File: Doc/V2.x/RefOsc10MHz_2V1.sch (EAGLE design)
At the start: 82 parts, among them CON1 TYCO-AMP_USBUSB-B_SMT, CON2 HEADER-2X5SMD, CON3 SD-73100-0105, CON4 AVR-ISP-6SMD, CON5 AVR-JTAG-10SMD, CON6 HEADER-2X3SMD, CON7 MCX-J-P-X-RA-SM1, IC1 ATmega328-P, IC2 LC4032V_XXT44, IC3 74HCT221D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

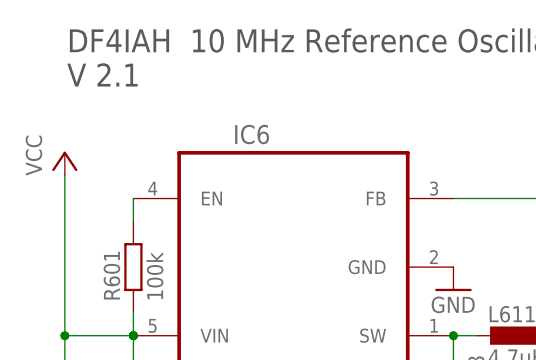
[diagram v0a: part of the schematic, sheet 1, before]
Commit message: avr_DF4IAH_Bootloader - Doc - Eagle: V2.1 - correction: CRS80 --> CRS08 (2)
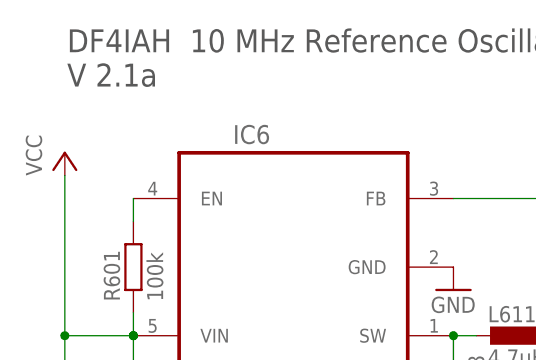
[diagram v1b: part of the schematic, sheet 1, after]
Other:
- note added: "DF4IAH 10 MHz Reference Oscillator V 2.1a"
- note removed: "DF4IAH 10 MHz Reference Oscillator V 2.1"
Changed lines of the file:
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@@
 <text x="198.12" y="145.034" size="1.016" layer="97">2.5 MHz out</text>
 <text x="5.334" y="291.846" size="2.54" layer="97">DF4IAH  10 MHz Reference Oscillator
-V 2.1</text>
+V 2.1a</text>
 <text x="59.436" y="144.018" size="1.778" layer="97">USB Disconnect</text>
 <text x="102.616" y="122.936" size="1.778" layer="97">USB D-</text>

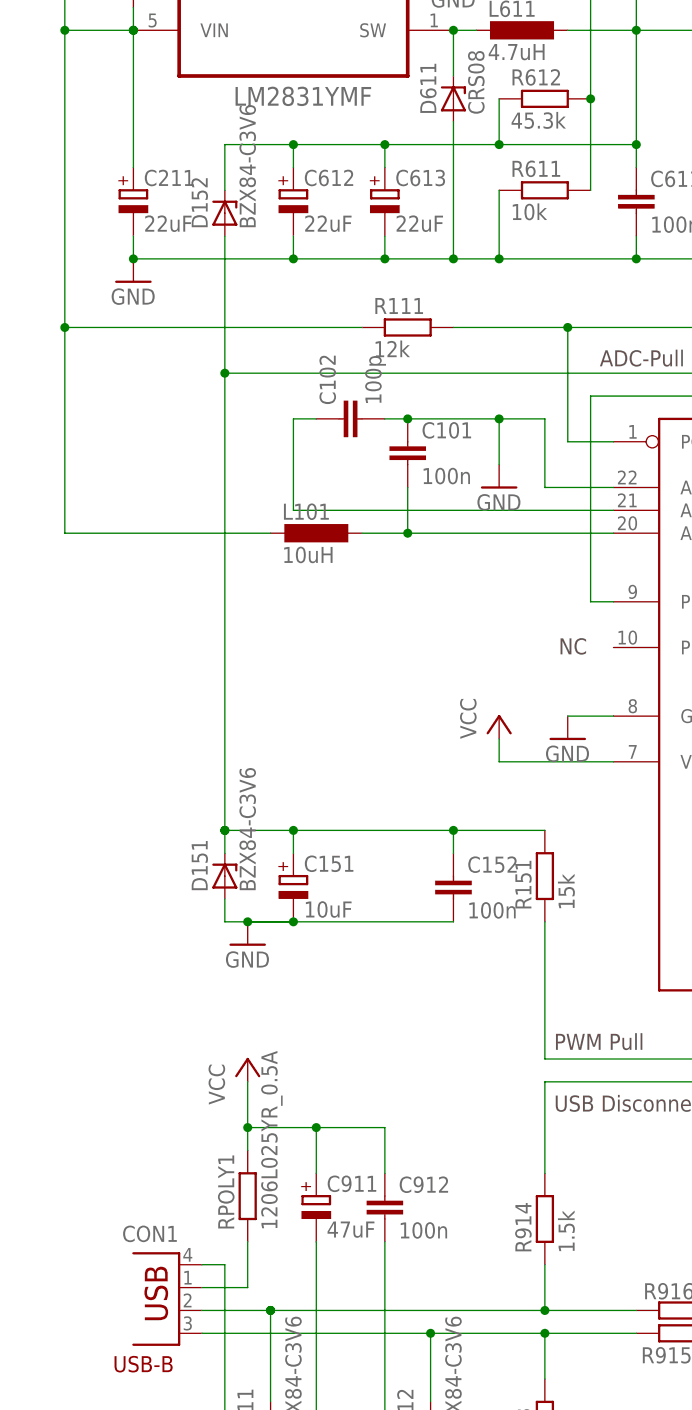
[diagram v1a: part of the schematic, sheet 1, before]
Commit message: avr_DF4IAH_Bootloader - Doc - Eagle: V2.1/V2.2 - removed elkos and replaced it by C0805 MLCCs
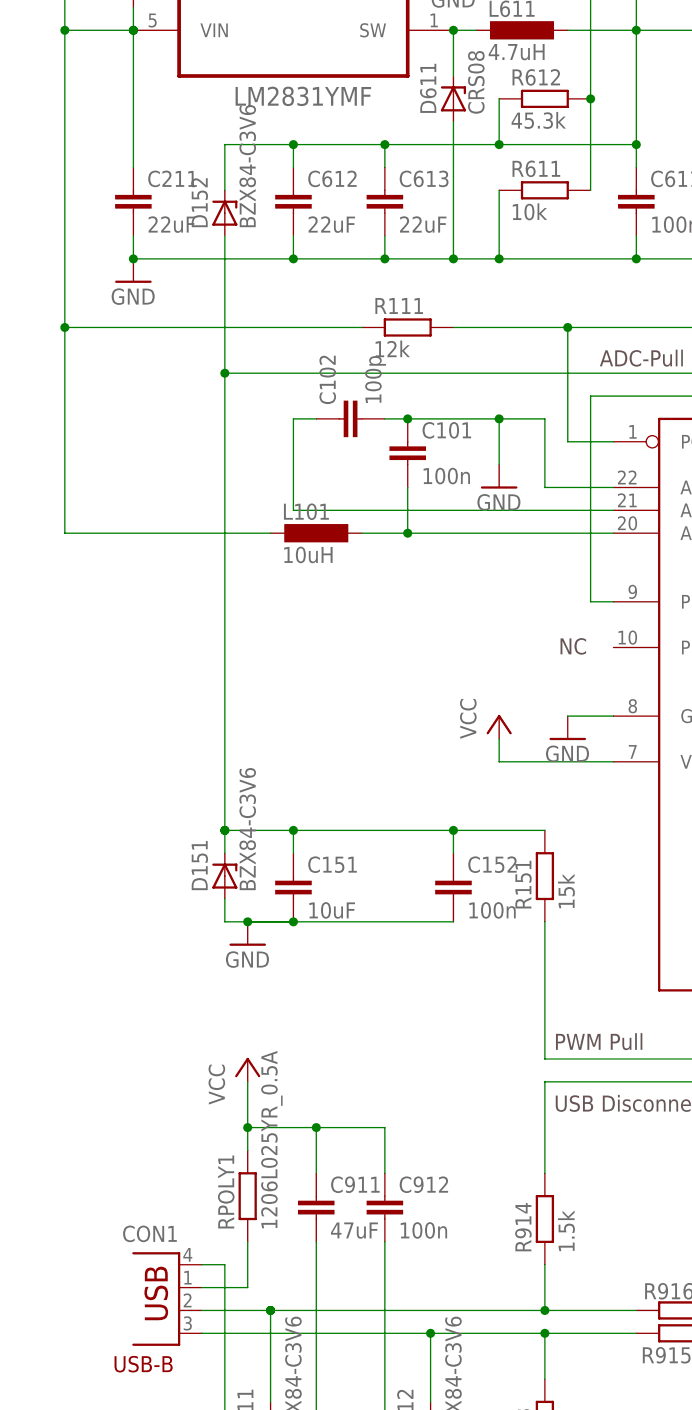
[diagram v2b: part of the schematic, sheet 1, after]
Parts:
- C151, C211, C612, C613: device rcl:CPOL-EUB -> rcl:C-EUC0805
- C911: device rcl:CPOL-EUC -> rcl:C-EUC0805
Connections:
- net +3V3: now also C612.1, C613.1; no longer C612.+, C613.+
- net GND: now also C151.2, C211.2, C612.2, C613.2, C911.2; no longer C151.-, C211.-, C612.-, C613.-, C911.-
- net N_ADC_PULL: now also C151.1; no longer C151.+
- net VCC: now also C211.1, C911.1; no longer C211.+, C911.+
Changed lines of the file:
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@@
 <part name="P+12" library="supply1" deviceset="VCC" device=""/>
 <part name="GND16" library="supply1" deviceset="GND" device=""/>
-<part name="C911" library="rcl" deviceset="CPOL-EU" device="C" value="47uF"/>
+<part name="C911" library="rcl" deviceset="C-EU" device="C0805" value="47uF"/>
 <part name="D911" library="diode" deviceset="BZX84CSMD" device="" value="BZX84-C3V6"/>
 <part name="D912" library="diode" deviceset="BZX84CSMD" device="" value="BZX84-C3V6"/>
@@
 <part name="C391" library="rcl" deviceset="C-EU" device="C0805" value="100n"/>
 <part name="C591" library="rcl" deviceset="C-EU" device="C0805" value="10n"/>
-<part name="C151" library="rcl" deviceset="CPOL-EU" device="B" value="10uF"/>
+<part name="C151" library="rcl" deviceset="C-EU" device="C0805" value="10uF"/>
 <part name="R612" library="rcl" deviceset="R-EU_" device="R0805" value="45.3k"/>
 <part name="R611" library="rcl" deviceset="R-EU_" device="R0805" value="10k"/>
@@
 <part name="R132" library="rcl" deviceset="R-EU_" device="R0805" value="47k"/>
 <part name="R311" library="rcl" deviceset="R-EU_" device="R0805" value="4.7k"/>
-<part name="C612" library="rcl" deviceset="CPOL-EU" device="B" value="22uF"/>
-<part name="C613" library="rcl" deviceset="CPOL-EU" device="B" value="22uF"/>
-<part name="C211" library="rcl" deviceset="CPOL-EU" device="B" value="22uF"/>
+<part name="C612" library="rcl" deviceset="C-EU" device="C0805" value="22uF"/>
+<part name="C613" library="rcl" deviceset="C-EU" device="C0805" value="22uF"/>
+<part name="C211" library="rcl" deviceset="C-EU" device="C0805" value="22uF"/>
 </parts>
 <sheets>
@@
 <pinref part="D151" gate="G$1" pin="A"/>
 <pinref part="C152" gate="G$1" pin="2"/>
-<pinref part="C151" gate="G$1" pin="-"/>
+<pinref part="C151" gate="G$1" pin="2"/>
 <junction x="30.48" y="165.1"/>
 </segment>
@@
 <pinref part="IC7" gate="&gt;NAME" pin="GND"/>
 <pinref part="D611" gate="G$1" pin="A"/>
-<pinref part="C612" gate="G$1" pin="-"/>
-<pinref part="C613" gate="G$1" pin="-"/>
-<pinref part="C211" gate="G$1" pin="-"/>
+<pinref part="C612" gate="G$1" pin="2"/>
+<pinref part="C613" gate="G$1" pin="2"/>
+<pinref part="C211" gate="G$1" pin="2"/>
 </segment>
 <segment>
@@
 <pinref part="GND1" gate="1" pin="GND"/>
 <wire x1="22.86" y1="99.06" x2="22.86" y2="104.14" width="0.1524" layer="91"/>
-<pinref part="C911" gate="G$1" pin="-"/>
+<pinref part="C911" gate="G$1" pin="2"/>
 <pinref part="D911" gate="G$1" pin="A"/>
 <pinref part="D912" gate="G$1" pin="A"/>
@@
 <pinref part="L101" gate="G$1" pin="2"/>
 <pinref part="IC6" gate="A" pin="VIN"/>
-<pinref part="C211" gate="G$1" pin="+"/>
+<pinref part="C211" gate="G$1" pin="1"/>
 </segment>
 <segment>
@@
 <wire x1="25.4" y1="147.32" x2="25.4" y2="142.24" width="0.1524" layer="91"/>
 <junction x="25.4" y="142.24"/>
-<pinref part="C911" gate="G$1" pin="+"/>
+<pinref part="C911" gate="G$1" pin="1"/>
 <pinref part="RPOLY1" gate="G$1" pin="2"/>
 <pinref part="C912" gate="G$1" pin="1"/>
@@
 <junction x="30.48" y="175.26"/>
 <pinref part="R151" gate="G$1" pin="2"/>
-<pinref part="C151" gate="G$1" pin="+"/>
+<pinref part="C151" gate="G$1" pin="1"/>
 <pinref part="IC7" gate="&gt;NAME" pin="VC"/>
 <pinref part="D152" gate="G$1" pin="A"/>
@@
 <junction x="121.92" y="264.16"/>
 <pinref part="R701" gate="G$1" pin="1"/>
-<pinref part="C612" gate="G$1" pin="+"/>
-<pinref part="C613" gate="G$1" pin="+"/>
-</segment>
-</net>
+<pinref part="C612" gate="G$1" pin="1"/>
+<pinref part="C613" gate="G$1" pin="1"/>
+</segment>
+</net>

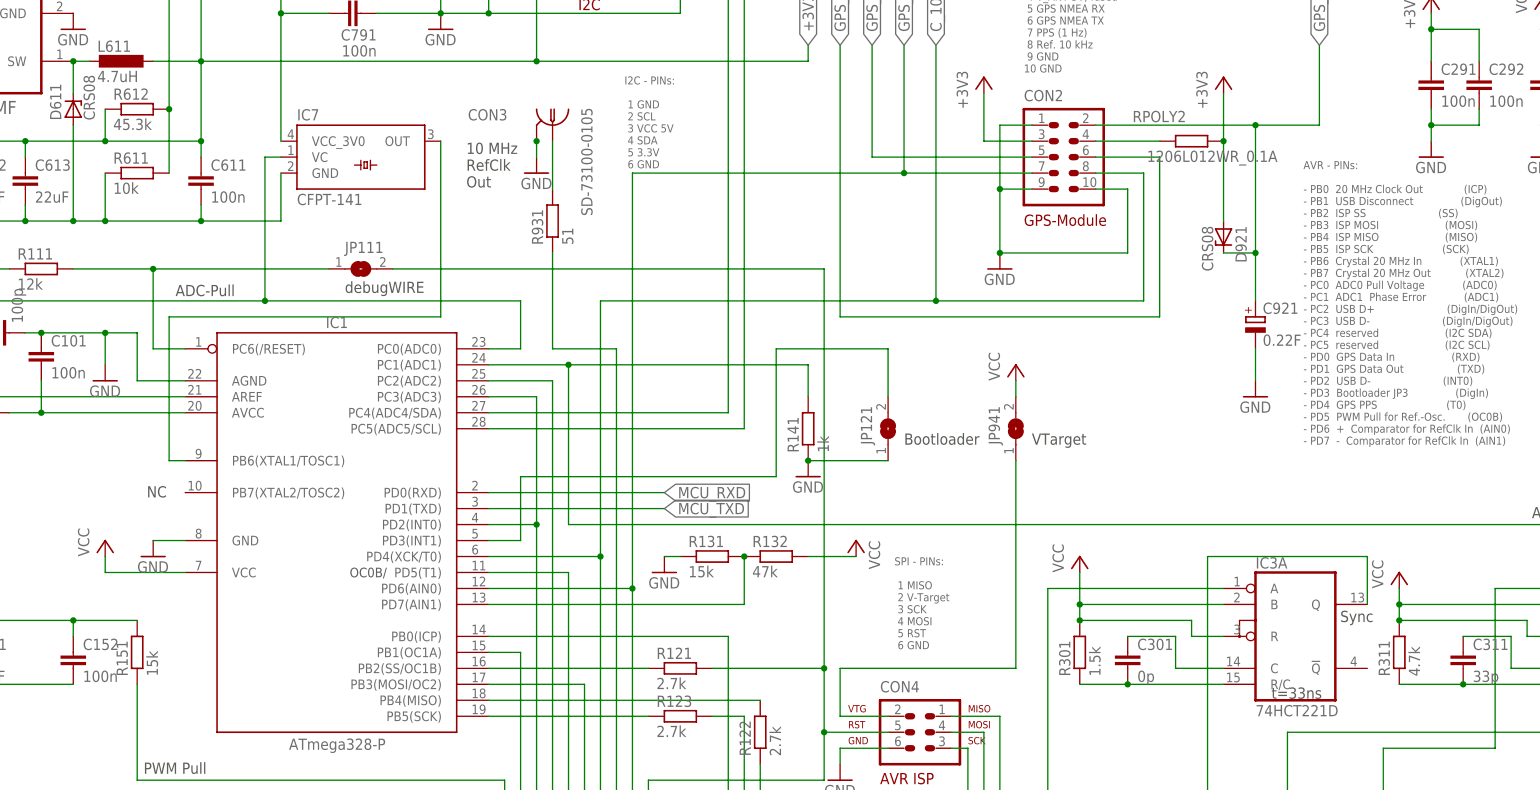
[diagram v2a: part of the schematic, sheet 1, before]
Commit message: avr_DF4IAH_Bootloader - Doc - Eagle: 2.1, 2.2, 2.3 - three resistors changed
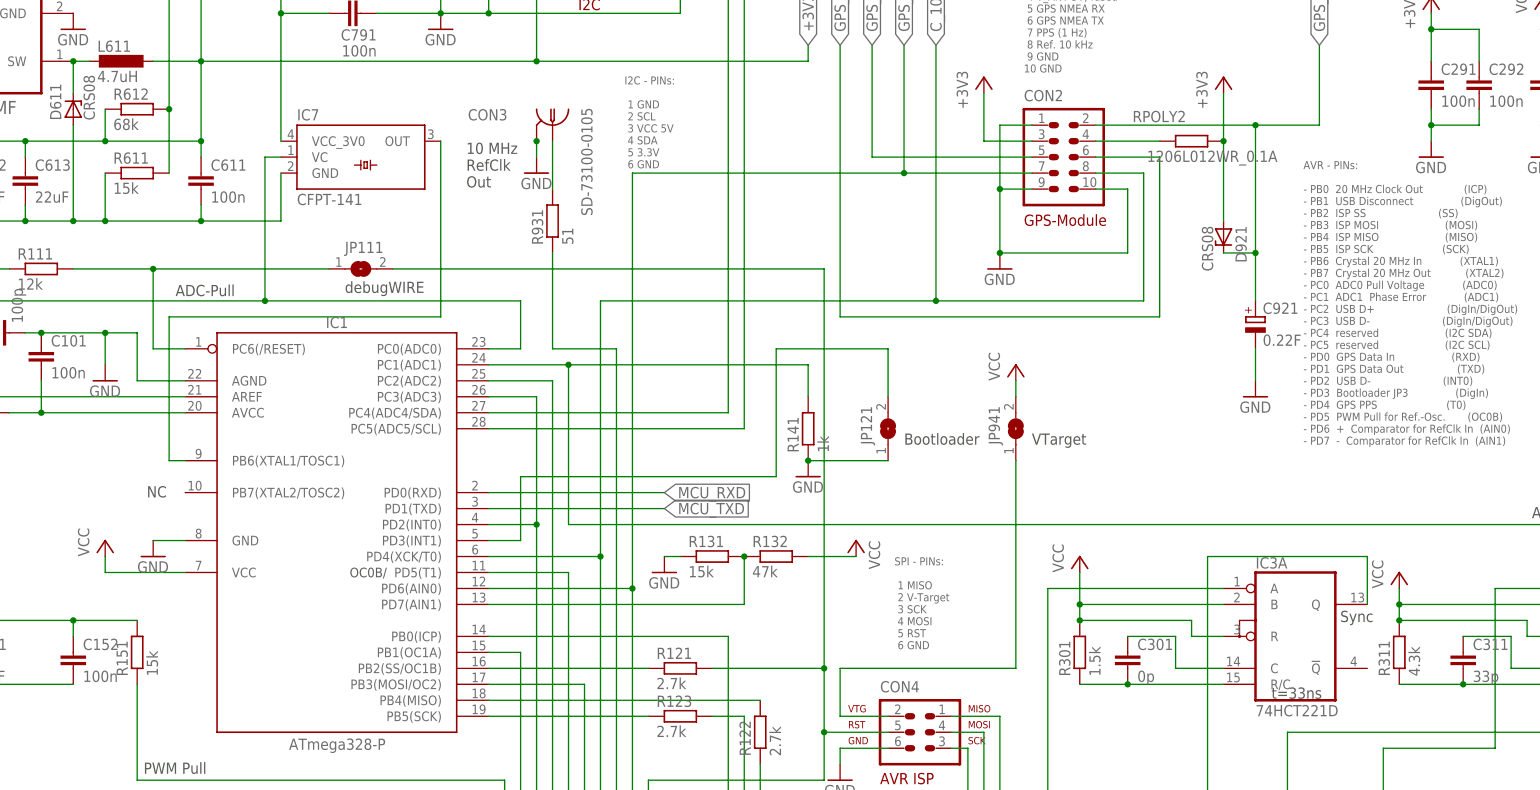
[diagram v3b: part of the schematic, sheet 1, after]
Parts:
- R311: value 4.7k -> 4.3k
- R611: value 10k -> 15k
- R612: value 45.3k -> 68k
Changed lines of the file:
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@@
 <part name="C591" library="rcl" deviceset="C-EU" device="C0805" value="10n"/>
 <part name="C151" library="rcl" deviceset="C-EU" device="C0805" value="10uF"/>
-<part name="R612" library="rcl" deviceset="R-EU_" device="R0805" value="45.3k"/>
-<part name="R611" library="rcl" deviceset="R-EU_" device="R0805" value="10k"/>
+<part name="R612" library="rcl" deviceset="R-EU_" device="R0805" value="68k"/>
+<part name="R611" library="rcl" deviceset="R-EU_" device="R0805" value="15k"/>
 <part name="R601" library="rcl" deviceset="R-EU_" device="R0805" value="100k"/>
 <part name="L611" library="rcl" deviceset="L-EU" device="L5650M" value="4.7uH"/>
@@
 <part name="R131" library="rcl" deviceset="R-EU_" device="R0805" value="15k"/>
 <part name="R132" library="rcl" deviceset="R-EU_" device="R0805" value="47k"/>
-<part name="R311" library="rcl" deviceset="R-EU_" device="R0805" value="4.7k"/>
+<part name="R311" library="rcl" deviceset="R-EU_" device="R0805" value="4.3k"/>
 <part name="C612" library="rcl" deviceset="C-EU" device="C0805" value="22uF"/>
 <part name="C613" library="rcl" deviceset="C-EU" device="C0805" value="22uF"/>
